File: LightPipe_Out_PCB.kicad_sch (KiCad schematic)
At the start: 10 parts, among them X1 Conn_01x04, X2 Conn_01x04, X3 Conn_01x02, X4.1 Conn_01x01, X4.2 Conn_01x01, X5.1 Conn_01x01, X5.2 Conn_01x01

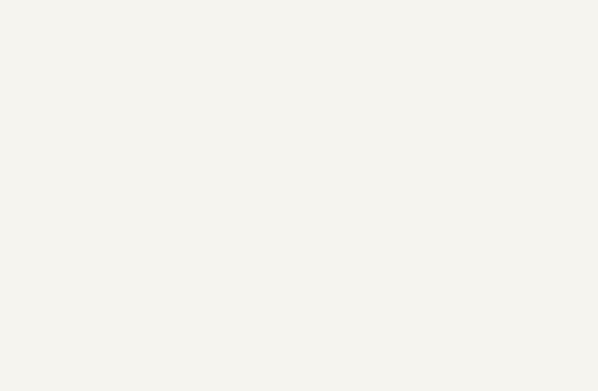
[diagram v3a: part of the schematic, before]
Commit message: [QR] Added QR-Code to schematic | defined QR-Code on Board to be not on schematic
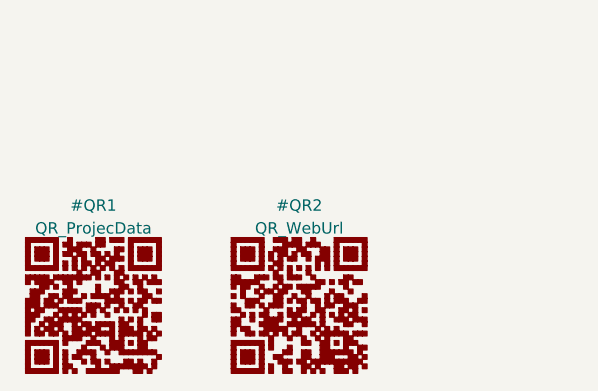
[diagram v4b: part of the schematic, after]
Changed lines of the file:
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@@
     (pin "1")
+  )
+  (symbol (lib_id "QR_Lib:QR_ProjecData") (at 27.94 184.15 0) (unit 1)
+    (in_bom no) (on_board yes) (fields_autoplaced)
+    (property "Reference" "#QR1" (id 0) (at 27.98 173.0767 0))
+    (property "Value" "QR_ProjecData" (id 1) (at 27.98 175.6136 0))
+    (property "Footprint" "QR:QR_ProjecData" (id 2) (at 27.94 194.6 0)
+      (effects (font (size 1.27 1.27)) hide)
+    )
+    (property "Datasheet" "" (id 3) (at 27.94 196.3 0)
+      (effects (font (size 1.27 1.27)) hide)
+    )
+    (property "qr_version" "3" (id 4) (at 27.94 198 0)
+      (effects (font (size 1.27 1.27)) hide)
+    )
+    (property "qr_size" "29" (id 5) (at 27.94 199.7 0)
+      (effects (font (size 1.27 1.27)) hide)
+    )
+    (property "qr_ecc" "0,1" (id 6) (at 27.94 201.4 0)
+      (effects (font (size 1.27 1.27)) hide)
+    )
+    (property "qr_mask" "2" (id 7) (at 27.94 203.1 0)
+      (effects (font (size 1.27 1.27)) hide)
+    )
+    (property "qr_text" "LightPipe - StripeConnector v0.1.0 CCC Göttingen" (id 8) (at 27.94 204.8 0)
+      (effects (font (size 1.27 1.27)) hide)
+    )
+  )
+  (symbol (lib_id "QR_Lib:QR_WebUrl") (at 50.8 184.15 0) (unit 1)
+    (in_bom no) (on_board yes) (fields_autoplaced)
+    (property "Reference" "#QR2" (id 0) (at 50.84 173.0767 0))
+    (property "Value" "QR_WebUrl" (id 1) (at 50.84 175.6136 0))
+    (property "Footprint" "QR:QR_WebUrl" (id 2) (at 50.8 194.6 0)
+      (effects (font (size 1.27 1.27)) hide)
+    )
+    (property "Datasheet" "" (id 3) (at 50.8 196.3 0)
+      (effects (font (size 1.27 1.27)) hide)
+    )
+    (property "qr_version" "3" (id 4) (at 50.8 198 0)
+      (effects (font (size 1.27 1.27)) hide)
+    )
+    (property "qr_size" "29" (id 5) (at 50.8 199.7 0)
+      (effects (font (size 1.27 1.27)) hide)
+    )
+    (property "qr_ecc" "0,1" (id 6) (at 50.8 201.4 0)
+      (effects (font (size 1.27 1.27)) hide)
+    )
+    (property "qr_mask" "5" (id 7) (at 50.8 203.1 0)
+      (effects (font (size 1.27 1.27)) hide)
+    )
+    (property "qr_text" "https://github.com/HansAchterbahn/LightPipe" (id 8) (at 50.8 204.8 0)
+      (effects (font (size 1.27 1.27)) hide)
+    )
   )
   (symbol (lib_id "Connector_Generic:Conn_01x01") (at 255.27 43.18 0) (unit 1)
@@
       (reference "#PWR0110") (unit 1) (value "+5V") (footprint "")
     )
+    (path "/8ca2c3de-1205-4532-8a76-d9c1a6b1f484"
+      (reference "#QR1") (unit 1) (value "QR_ProjecData") (footprint "QR:QR_ProjecData")
+    )
+    (path "/cb914536-84d3-4fd6-ba86-3661b57a5b27"
+      (reference "#QR2") (unit 1) (value "QR_WebUrl") (footprint "QR:QR_WebUrl")
+    )
     (path "/00000000-0000-0000-0000-00005f94ae24"

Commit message: [pcb] Optimized X1 and X2 positon
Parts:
- LD1, LD2, LD3: value Conn_01x04 -> APA102
- X1, X2: value Conn_01x04 -> KLB-4
- X3: value Conn_01x02 -> XT30
- X4.1, X4.2: value Conn_01x01 -> Cable-0.7mm
- X5.1, X5.2: value Conn_01x01 -> Cable-1.5mm
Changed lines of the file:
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@@
     (in_bom yes) (on_board yes)
     (property "Reference" "X3" (id 0) (at 80.01 99.06 0))
-    (property "Value" "Conn_01x02" (id 1) (at 82.042 107.5436 0)
+    (property "Value" "XT30" (id 1) (at 82.042 107.5436 0)
       (effects (font (size 1.27 1.27)) hide)
     )
@@
     (in_bom yes) (on_board yes)
     (property "Reference" "X5.2" (id 0) (at 166.37 105.41 0))
-    (property "Value" "Conn_01x01" (id 1) (at 168.402 104.5464 0)
+    (property "Value" "Cable-1.5mm" (id 1) (at 168.402 104.5464 0)
       (effects (font (size 1.27 1.27)) hide)
     )
@@
     (in_bom yes) (on_board yes)
     (property "Reference" "X5.1" (id 0) (at 166.37 97.79 0))
-    (property "Value" "Conn_01x01" (id 1) (at 168.402 96.9264 0)
+    (property "Value" "Cable-1.5mm" (id 1) (at 168.402 96.9264 0)
       (effects (font (size 1.27 1.27)) hide)
     )
@@
     (in_bom yes) (on_board yes)
     (property "Reference" "LD1" (id 0) (at 115.57 40.64 0))
-    (property "Value" "Conn_01x04" (id 1) (at 113.538 48.2346 0)
+    (property "Value" "APA102" (id 1) (at 113.538 48.2346 0)
       (effects (font (size 1.27 1.27)) (justify left) hide)
     )
@@
     (in_bom yes) (on_board yes)
     (property "Reference" "LD2" (id 0) (at 85.09 40.64 0))
-    (property "Value" "Conn_01x04" (id 1) (at 87.122 48.2346 0)
+    (property "Value" "APA102" (id 1) (at 87.122 48.2346 0)
       (effects (font (size 1.27 1.27)) (justify left) hide)
     )
@@
     (in_bom yes) (on_board yes)
     (property "Reference" "LD3" (id 0) (at 41.91 40.64 0))
-    (property "Value" "Conn_01x04" (id 1) (at 39.878 48.2346 0)
+    (property "Value" "APA102" (id 1) (at 39.878 48.2346 0)
       (effects (font (size 1.27 1.27)) (justify left) hide)
     )
@@
     (in_bom yes) (on_board yes)
     (property "Reference" "X4.2" (id 0) (at 255.27 48.26 0))
-    (property "Value" "Conn_01x01" (id 1) (at 253.238 54.2036 0)
+    (property "Value" "Cable-0.7mm" (id 1) (at 253.238 54.2036 0)
       (effects (font (size 1.27 1.27)) hide)
     )
@@
     (in_bom yes) (on_board yes)
     (property "Reference" "X1" (id 0) (at 165.1 40.64 0))
-    (property "Value" "Conn_01x04" (id 1) (at 167.132 48.6922 0)
+    (property "Value" "KLB-4" (id 1) (at 167.132 48.6922 0)
       (effects (font (size 1.27 1.27)) (justify left) hide)
     )
@@
     (in_bom yes) (on_board yes)
     (property "Reference" "X2" (id 0) (at 198.12 40.64 0))
-    (property "Value" "Conn_01x04" (id 1) (at 198.12 40.7471 0)
+    (property "Value" "KLB-4" (id 1) (at 198.12 40.7471 0)
       (effects (font (size 1.27 1.27)) hide)
     )
@@
     (in_bom yes) (on_board yes)
     (property "Reference" "X4.1" (id 0) (at 255.27 40.64 0))
-    (property "Value" "Conn_01x01" (id 1) (at 253.238 46.5836 0)
+    (property "Value" "Cable-0.7mm" (id 1) (at 253.238 46.5836 0)
       (effects (font (size 1.27 1.27)) hide)
     )
@@
     )
     (path "/00000000-0000-0000-0000-00005f94ae24"
-      (reference "LD1") (unit 1) (value "Conn_01x04") (footprint "h8-Connectors:APA102-Strip-Output")
+      (reference "LD1") (unit 1) (value "APA102") (footprint "h8-Connectors:APA102-Strip-Output")
     )
     (path "/00000000-0000-0000-0000-00005f94aec9"
-      (reference "LD2") (unit 1) (value "Conn_01x04") (footprint "h8-Connectors:APA102-Strip-Input")
+      (reference "LD2") (unit 1) (value "APA102") (footprint "h8-Connectors:APA102-Strip-Input")
     )
     (path "/00000000-0000-0000-0000-00005f94af29"
-      (reference "LD3") (unit 1) (value "Conn_01x04") (footprint "h8-Connectors:APA102-Strip-Output")
+      (reference "LD3") (unit 1) (value "APA102") (footprint "h8-Connectors:APA102-Strip-Output")
     )
     (path "/52137419-c203-4dbe-a47e-235ddc4fd115"
-      (reference "X1") (unit 1) (value "Conn_01x04") (footprint "h8-Connectors:Lumberg-KLB-4-Klinkensteckverbinder-3_5-180deg-turnable")
+      (reference "X1") (unit 1) (value "KLB-4") (footprint "h8-Connectors:Lumberg-KLB-4-Klinkensteckverbinder-3_5-180deg-turnable")
     )
     (path "/771c4cae-8f80-4832-b07b-977abc522dad"
-      (reference "X2") (unit 1) (value "Conn_01x04") (footprint "h8-Connectors:Lumberg-KLB-4-Klinkensteckverbinder-3_5-180deg-turnable")
+      (reference "X2") (unit 1) (value "KLB-4") (footprint "h8-Connectors:Lumberg-KLB-4-Klinkensteckverbinder-3_5-180deg-turnable")
     )
     (path "/00000000-0000-0000-0000-00005f94666b"
-      (reference "X3") (unit 1) (value "Conn_01x02") (footprint "h8-Connectors:XT30")
+      (reference "X3") (unit 1) (value "XT30") (footprint "h8-Connectors:XT30")
     )
     (path "/ea7784c2-710b-445a-ba50-3da775d876ed"
-      (reference "X4.1") (unit 1) (value "Conn_01x01") (footprint "h8-Connectors:Solder-Pad-THT-0.7mm")
+      (reference "X4.1") (unit 1) (value "Cable-0.7mm") (footprint "h8-Connectors:Solder-Pad-THT-0.7mm")
     )
     (path "/24cb6112-8d07-4162-b71e-d29d9e542042"
-      (reference "X4.2") (unit 1) (value "Conn_01x01") (footprint "h8-Connectors:Solder-Pad-THT-0.7mm")
+      (reference "X4.2") (unit 1) (value "Cable-0.7mm") (footprint "h8-Connectors:Solder-Pad-THT-0.7mm")
     )
     (path "/00000000-0000-0000-0000-00005f946830"
-      (reference "X5.1") (unit 1) (value "Conn_01x01") (footprint "h8-Connectors:Solder-Pad-THT-1.5mm")
+      (reference "X5.1") (unit 1) (value "Cable-1.5mm") (footprint "h8-Connectors:Solder-Pad-THT-1.5mm")
     )
     (path "/00000000-0000-0000-0000-00005f9467ba"
-      (reference "X5.2") (unit 1) (value "Conn_01x01") (footprint "h8-Connectors:Solder-Pad-THT-1.5mm")
-    )
-  )
+      (reference "X5.2") (unit 1) (value "Cable-1.5mm") (footprint "h8-Connectors:Solder-Pad-THT-1.5mm")
+    )
+  )
